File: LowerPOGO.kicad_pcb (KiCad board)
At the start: 2 copper layers, 116 x 67.1 mm, 29 parts, among them J1 Conn_01x01_MountingPin, J10 Conn_01x01_MountingPin, J11 Conn_01x01_MountingPin, J12 Conn_01x01_MountingPin, J13 Conn_01x01_MountingPin, J14 Conn_01x01_MountingPin, J15 Conn_01x01_MountingPin, J16 Conn_01x01_MountingPin, J17 Conn_01x01_MountingPin, J18 Conn_01x01_MountingPin, J19 Conn_01x01_MountingPin, J2 Conn_01x01_MountingPin, J20 Conn_01x01_MountingPin, J21 Conn_01x01_MountingPin, J22 Conn_01x01_MountingPin, J23 Conn_01x01_MountingPin, J24 Conn_01x01_MountingPin, J25 Conn_01x24_Pin, J3 Conn_01x01_MountingPin, J4 Conn_01x01_MountingPin, J5 Conn_01x01_MountingPin, J6 Conn_01x01_MountingPin, J7 Conn_01x01_MountingPin, J8 Conn_01x01_MountingPin, J9 Conn_01x01_MountingPin

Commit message: Update rev3 to modify J25 connector: Move J25 to be populated from the back of board Updated SVGs to show component 3D models Updated Fabrication Outputs
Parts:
- J25: moved to B.Cu
- moved J25 0.84 mm to (143.8, 91.7), turned to 180 degrees

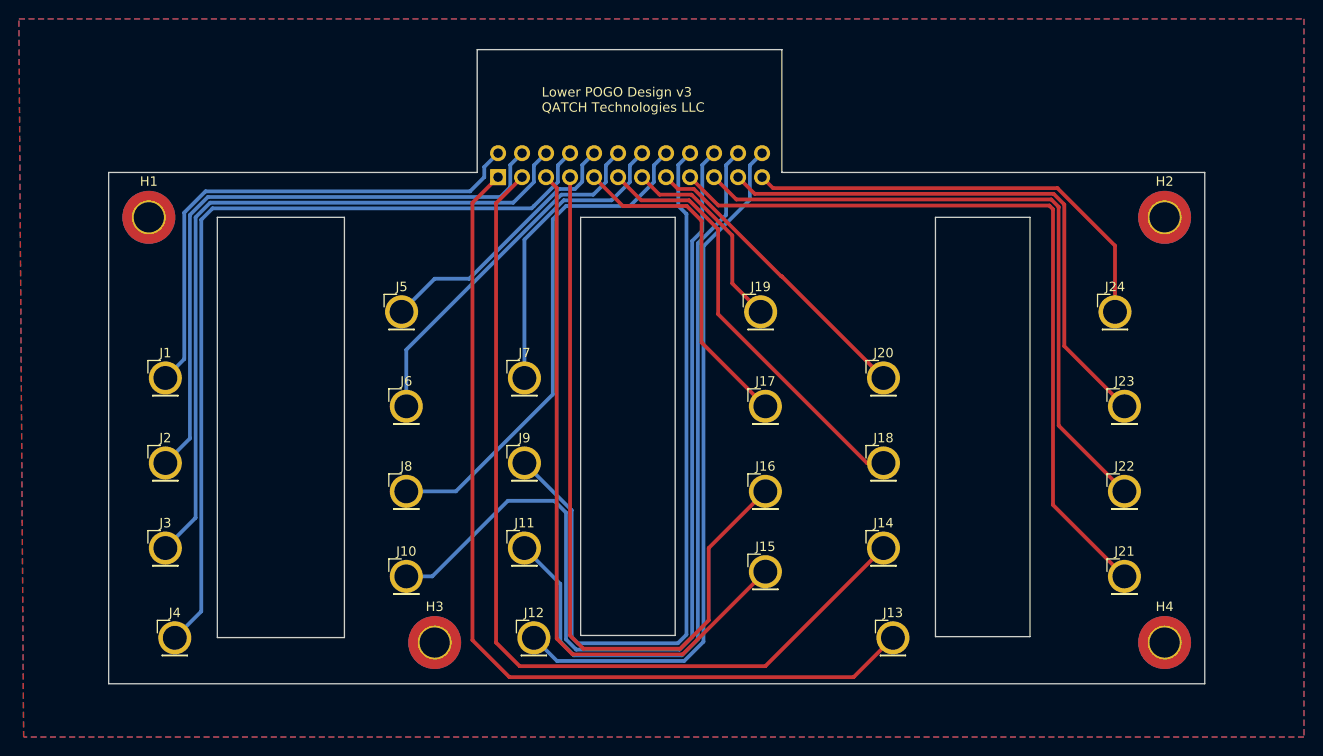
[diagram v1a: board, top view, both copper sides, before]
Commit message: LowerPOGO v4 (2024-06-21) Resize J vias for proper fit inner diameter: 2.49mm outer diameter: 3.25mm
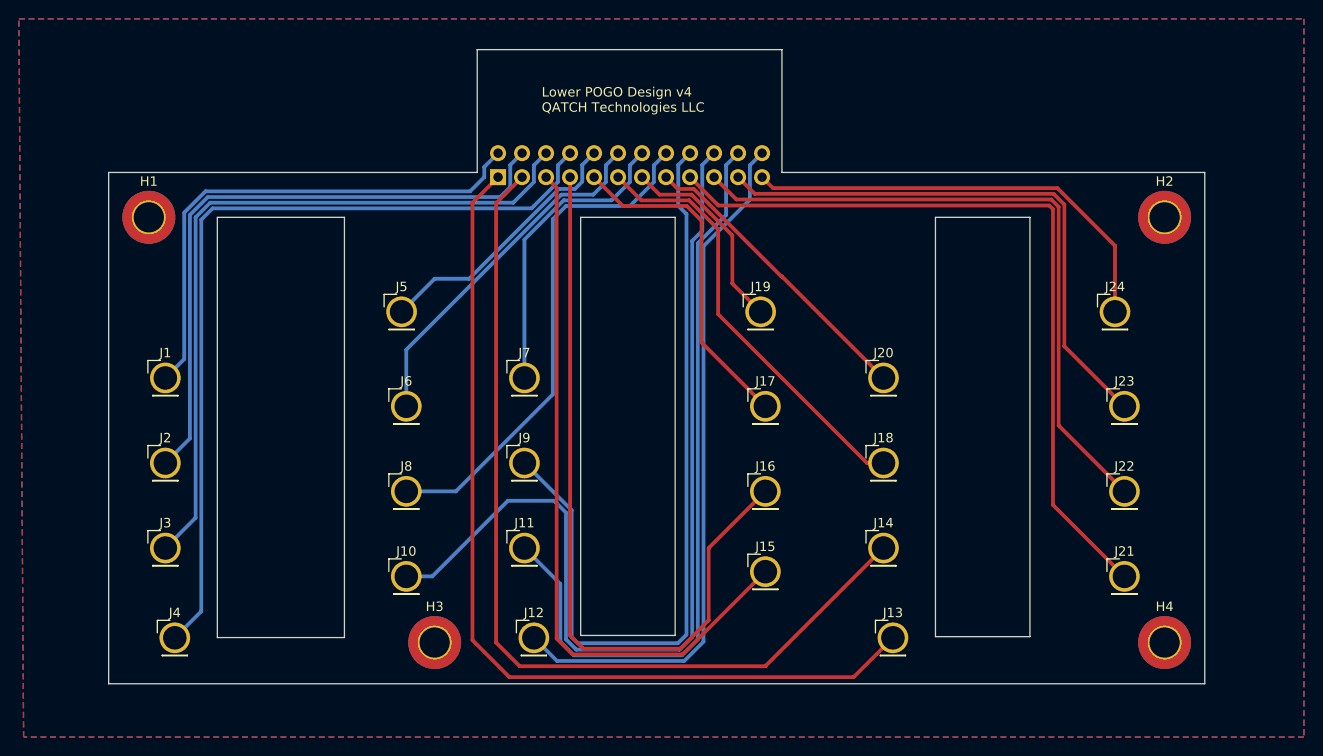
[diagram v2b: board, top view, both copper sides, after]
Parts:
- J1, J10, J11, J12, J13, J14, J15, J16, J17, J18, J19, J2, J20, J21, J22, J23, J24, J3, J4, J5, J6, J7, J8, J9: footprint Connector_PinHeader_2.54mm:PinHeader_1x01_D2.54mm_Vertical -> Connector_PinHeader_2.54mm:PinHeader_1x01_D2.54mm_Vertical_PogoPin
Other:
- board text added: "Lower POGO Design v4 QATCH Technologies LLC"
- board text removed: "Lower POGO Design v3 QATCH Technologies LLC"

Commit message: LowerPOGO v5 1mm trace spacing 1mm POGO clearance
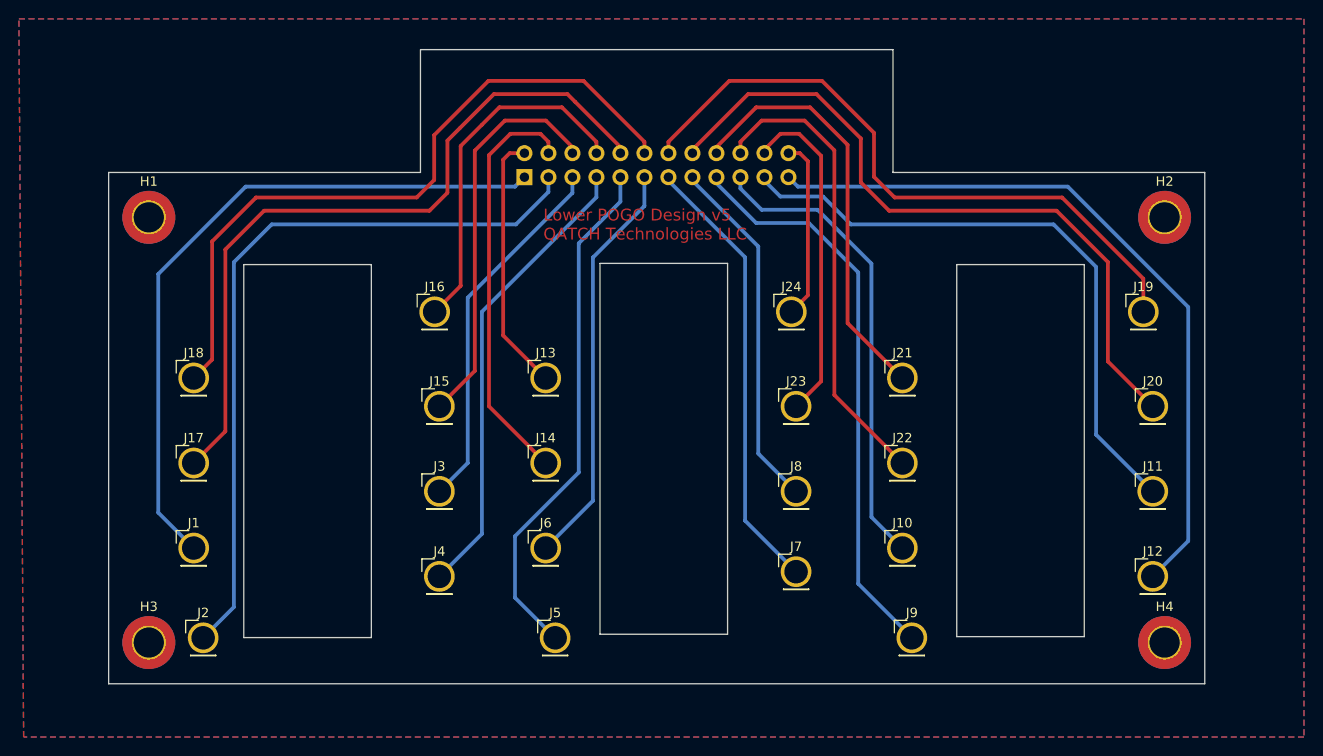
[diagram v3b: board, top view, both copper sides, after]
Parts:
- moved H3 30.2 mm to (93.2, 154.5)
- moved J15 3.50 mm to (124.0, 129.5)
- moved J16 3.50 mm to (123.5, 119.5)
- moved J3 3.50 mm to (124.0, 138.5)
- moved J4 3.50 mm to (124.0, 147.5)
- moved J23 3.25 mm to (161.8, 129.5)
- moved J24 3.25 mm to (161.2, 119.5)
- moved J7 3.25 mm to (161.8, 147.0)
- moved J8 3.25 mm to (161.8, 138.5)
- moved J1 3.00 mm to (98.0, 144.5)
- moved J11 3.00 mm to (199.5, 138.5)
- moved J12 3.00 mm to (199.5, 147.5)
- moved J17 3.00 mm to (98.0, 135.5)
- moved J18 3.00 mm to (98.0, 126.5)
- moved J19 3.00 mm to (198.5, 119.5)
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- renumbered J3 to J1, J14 to J10, J22 to J11, J21 to J12, J7 to J13, J9 to J14, J6 to J15, J5 to J16, J2 to J17, J1 to J18, J24 to J19, J4 to J2, J23 to J20, J20 to J21, J18 to J22, J17 to J23, J19 to J24, J8 to J3, J10 to J4, J12 to J5, J11 to J6, J15 to J7, J16 to J8, J13 to J9
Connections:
- J1 pad 1: Net-(J25-Pin_3) -> Net-(J1-Pin_1)
- J10 pad 1: Net-(J14-Pin_1) -> Net-(J10-Pin_1)
- J11 pad 1: Net-(J22-Pin_1) -> Net-(J11-Pin_1)
- J12 pad 1: Net-(J21-Pin_1) -> Net-(J12-Pin_1)
- J13 pad 1: Net-(J25-Pin_7) -> Net-(J13-Pin_1)
- J14 pad 1: Net-(J25-Pin_9) -> Net-(J14-Pin_1)
- J15 pad 1: Net-(J25-Pin_6) -> Net-(J15-Pin_1)
- J16 pad 1: Net-(J25-Pin_5) -> Net-(J16-Pin_1)
- J17 pad 1: Net-(J2-Pin_1) -> Net-(J17-Pin_1)
- J18 pad 1: Net-(J1-Pin_1) -> Net-(J18-Pin_1)
- J19 pad 1: Net-(J24-Pin_1) -> Net-(J19-Pin_1)
- J2 pad 1: Net-(J25-Pin_4) -> Net-(J2-Pin_1)
- J20 pad 1: Net-(J23-Pin_1) -> Net-(J20-Pin_1)
- J21 pad 1: Net-(J20-Pin_1) -> Net-(J21-Pin_1)
- J22 pad 1: Net-(J18-Pin_1) -> Net-(J22-Pin_1)
- J23 pad 1: Net-(J17-Pin_1) -> Net-(J23-Pin_1)
- J24 pad 1: Net-(J19-Pin_1) -> Net-(J24-Pin_1)
- J3 pad 1: Net-(J25-Pin_8) -> Net-(J25-Pin_3)
- J4 pad 1: Net-(J10-Pin_1) -> Net-(J25-Pin_4)
- J5 pad 1: Net-(J12-Pin_1) -> Net-(J25-Pin_5)
- J6 pad 1: Net-(J11-Pin_1) -> Net-(J25-Pin_6)
- J7 pad 1: Net-(J15-Pin_1) -> Net-(J25-Pin_7)
- J8 pad 1: Net-(J16-Pin_1) -> Net-(J25-Pin_8)
- J9 pad 1: Net-(J13-Pin_1) -> Net-(J25-Pin_9)
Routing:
- net Net-(J13-Pin_1): track 98.0 -> 27.6 mm
- net Net-(J14-Pin_1): track 97.6 -> 43.8 mm
- net Net-(J10-Pin_1): track 100.7 -> 49.8 mm
- net Net-(J19-Pin_1): track 21.4 -> 69.0 mm
- net Net-(J16-Pin_1): track 81.1 -> 37.5 mm
- net Net-(J17-Pin_1): track 35.7 -> 78.8 mm
- net Net-(J20-Pin_1): track 31.8 -> 74.1 mm
- net Net-(J25-Pin_4): track 88.4 -> 49.1 mm
- net Net-(J25-Pin_3): track 77.3 -> 39.1 mm
- net Net-(J21-Pin_1): track 81.8 -> 45.0 mm
- net Net-(J15-Pin_1): track 75.7 -> 42.1 mm
- net Net-(J18-Pin_1): track 45.9 -> 74.7 mm
- net Net-(J24-Pin_1): track 47.4 -> 19.1 mm
- net Net-(J25-Pin_5): track 28.4 -> 55.1 mm
- net Net-(J25-Pin_9): track 85.1 -> 60.6 mm
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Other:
- outline, holes or cut-outs redrawn
- board text added: "Lower POGO Design v5 QATCH Technologies LLC"
- board text removed: "Lower POGO Design v4 QATCH Technologies LLC"

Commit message: Changes for LowerPOGO v6: - Move the 3 cutouts left 2.5mm - Reduce cutout height by 1.5mm - Move center port right 0.25mm - Move traces for moved cutouts - Set clearance to avoid island - Update version text to "v6" - Update fabrication outputs - Update dimensional drawing
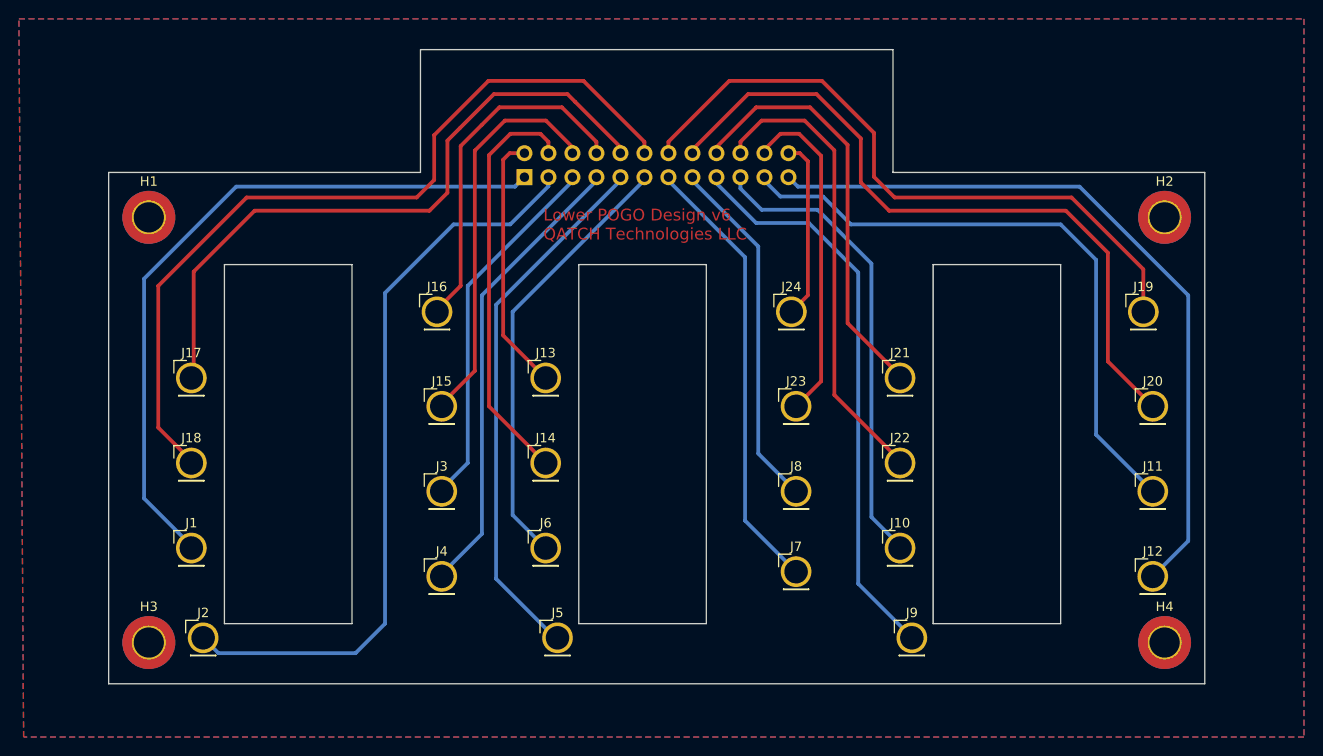
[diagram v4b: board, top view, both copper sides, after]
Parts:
- moved J1 0.25 mm to (97.8, 144.5)
- moved J10 0.25 mm to (172.8, 144.5)
- moved J15 0.25 mm to (124.2, 129.5)
- moved J16 0.25 mm to (123.8, 119.5)
- moved J17 0.25 mm to (97.8, 126.5)
- moved J18 0.25 mm to (97.8, 135.5)
- moved J21 0.25 mm to (172.8, 126.5)
- moved J22 0.25 mm to (172.8, 135.5)
- moved J3 0.25 mm to (124.2, 138.5)
- moved J4 0.25 mm to (124.2, 147.5)
- moved J5 0.25 mm to (136.5, 154.0)
- renumbered J18 to J17, J17 to J18
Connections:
- J17 pad 1: Net-(J18-Pin_1) -> Net-(J17-Pin_1)
- J18 pad 1: Net-(J17-Pin_1) -> Net-(J18-Pin_1)
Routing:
- net Net-(J18-Pin_1): track 74.7 -> 87.4 mm
- net Net-(J17-Pin_1): track 78.8 -> 70.4 mm
- net Net-(J25-Pin_6): track 43.6 -> 46.5 mm
- net Net-(J1-Pin_1): track 73.5 -> 75.4 mm
- net Net-(J25-Pin_5): track 55.1 -> 56.8 mm
- net Net-(J12-Pin_1): track 78.1 -> 78.8 mm
- net Net-(J19-Pin_1): track 69.0 -> 69.6 mm
- net Net-(J20-Pin_1): track 74.1 -> 74.7 mm
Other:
- outline, holes or cut-outs redrawn
- board text added: "Lower POGO Design v6 QATCH Technologies LLC"
- board text removed: "Lower POGO Design v5 QATCH Technologies LLC"

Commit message: Pushing local changes before branching
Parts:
- moved J25 2.21 mm to (146.5, 89.5)
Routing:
- net Net-(J22-Pin_1): track 49.5 -> 51.7 mm
- net Net-(J25-Pin_9): track 60.6 -> 62.8 mm
- net Net-(J25-Pin_7): track 47.3 -> 49.6 mm
- net Net-(J12-Pin_1): track 78.8 -> 81.0 mm
- net Net-(J11-Pin_1): track 65.9 -> 68.1 mm
- net Net-(J25-Pin_8): track 37.8 -> 40.0 mm
- net Net-(J25-Pin_6): track 46.5 -> 48.7 mm
- net Net-(J25-Pin_4): track 49.1 -> 51.3 mm
- net Net-(J25-Pin_3): track 39.1 -> 41.3 mm
- net Net-(J1-Pin_1): track 75.4 -> 77.6 mm
- net Net-(J25-Pin_5): track 56.8 -> 59.0 mm
- net Net-(J18-Pin_1): track 87.4 -> 89.6 mm
- net Net-(J21-Pin_1): track 45.0 -> 47.2 mm
- net Net-(J16-Pin_1): track 37.5 -> 39.6 mm
- net Net-(J15-Pin_1): track 42.1 -> 44.2 mm
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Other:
- board size 116 x 67.1 mm -> 116 x 69 mm

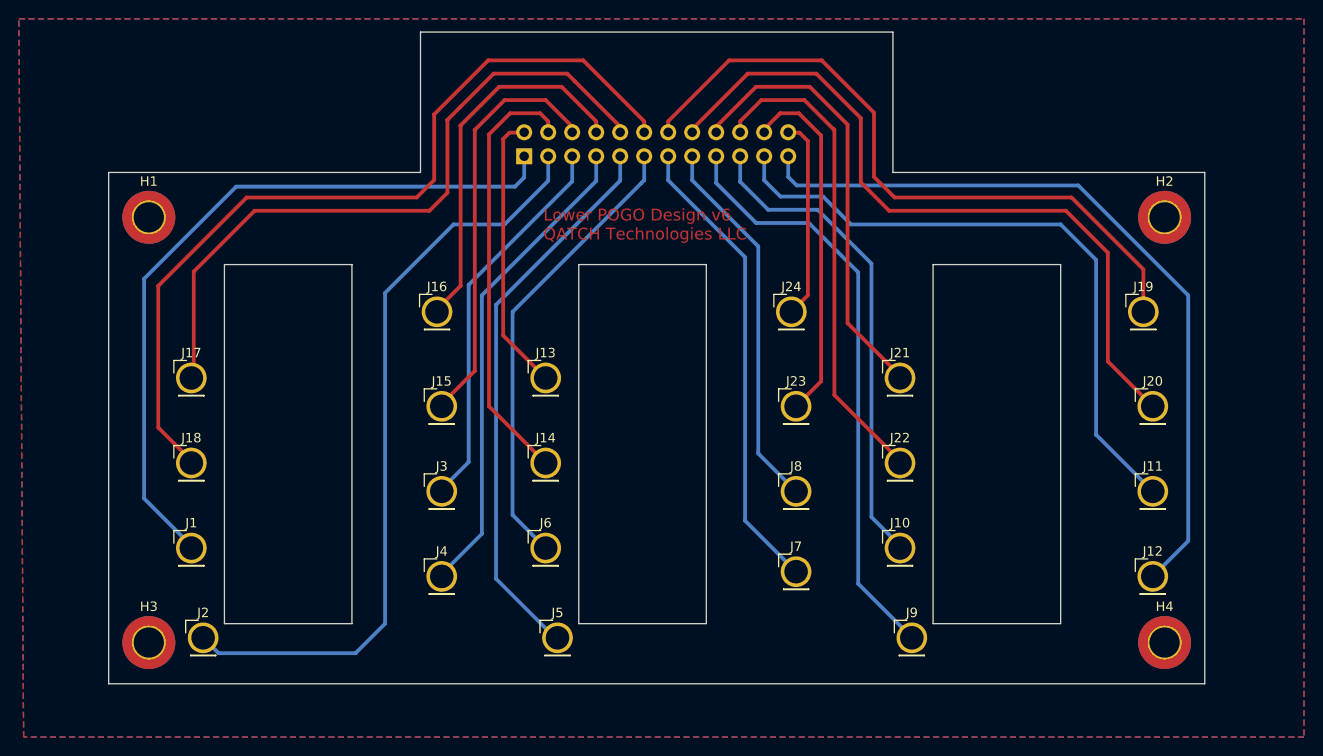
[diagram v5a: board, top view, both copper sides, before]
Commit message: Update KiCad designs for LowerPOGO to Multiport Design (v7) Tag fabrication outputs for this revision, remove Drawings.
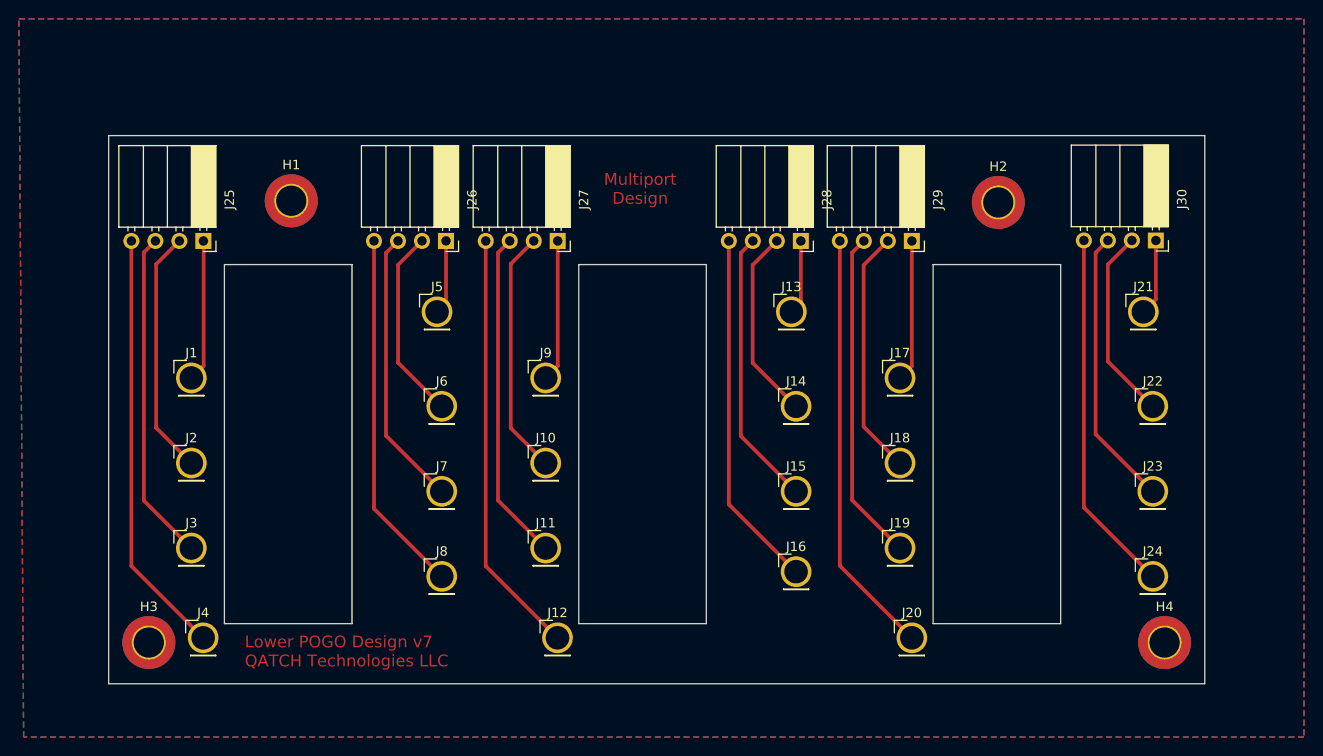
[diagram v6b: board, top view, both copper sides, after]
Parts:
- added J26: Conn_01x04_Pin, Connector_PinSocket_2.54mm:PinSocket_1x04_P2.54mm_Horizontal, F.Cu at (124.7, 112.0)
- added J27: Conn_01x04_Pin, Connector_PinSocket_2.54mm:PinSocket_1x04_P2.54mm_Horizontal, F.Cu at (136.5, 112.0)
- added J28: Conn_01x04_Pin, Connector_PinSocket_2.54mm:PinSocket_1x04_P2.54mm_Horizontal, F.Cu at (162.2, 112.0)
- added J29: Conn_01x04_Pin, Connector_PinSocket_2.54mm:PinSocket_1x04_P2.54mm_Horizontal, F.Cu at (174.0, 112.0)
- added J30: Conn_01x04_Pin, Connector_PinSocket_2.54mm:PinSocket_1x04_P2.54mm_Horizontal, F.Cu at (199.8, 112.0)
- J25: value Conn_01x24_Pin -> Conn_01x04_Pin; footprint Connector_PinSocket_2.54mm:PinSocket_2x12_P2.54mm_Horizontal -> Connector_PinSocket_2.54mm:PinSocket_1x04_P2.54mm_Horizontal; moved to F.Cu
- moved J25 52.6 mm to (99.0, 112.0), turned to -90 degrees
- moved H2 17.7 mm to (183.2, 107.9)
- moved H1 15.2 mm to (108.3, 107.8)
- renumbered J17 to J1, J14 to J10, J6 to J11, J5 to J12, J24 to J13, J23 to J14, J8 to J15, J7 to J16, J21 to J17, J22 to J18, J10 to J19, J18 to J2, J9 to J20, J19 to J21, J20 to J22, J11 to J23, J12 to J24, J1 to J3, J2 to J4, J16 to J5, J15 to J6, J3 to J7, J4 to J8, J13 to J9
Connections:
- J1 pad 1: Net-(J17-Pin_1) -> Net-(J1-Pin_1)
- J10 pad 1: Net-(J14-Pin_1) -> Net-(J10-Pin_1)
- J11 pad 1: Net-(J25-Pin_6) -> Net-(J11-Pin_1)
- J12 pad 1: Net-(J25-Pin_5) -> Net-(J12-Pin_1)
- J13 pad 1: Net-(J24-Pin_1) -> Net-(J13-Pin_1)
- J14 pad 1: Net-(J23-Pin_1) -> Net-(J14-Pin_1)
- J15 pad 1: Net-(J25-Pin_8) -> Net-(J15-Pin_1)
- J16 pad 1: Net-(J25-Pin_7) -> Net-(J16-Pin_1)
- J17 pad 1: Net-(J21-Pin_1) -> Net-(J17-Pin_1)
- J18 pad 1: Net-(J22-Pin_1) -> Net-(J18-Pin_1)
- J19 pad 1: Net-(J10-Pin_1) -> Net-(J19-Pin_1)
- J2 pad 1: Net-(J18-Pin_1) -> Net-(J2-Pin_1)
- J20 pad 1: Net-(J25-Pin_9) -> Net-(J20-Pin_1)
- J21 pad 1: Net-(J19-Pin_1) -> Net-(J21-Pin_1)
- J22 pad 1: Net-(J20-Pin_1) -> Net-(J22-Pin_1)
- J23 pad 1: Net-(J11-Pin_1) -> Net-(J23-Pin_1)
- J24 pad 1: Net-(J12-Pin_1) -> Net-(J24-Pin_1)
- J3 pad 1: Net-(J1-Pin_1) -> Net-(J25-Pin_3)
- J4 pad 1: Net-(J2-Pin_1) -> Net-(J25-Pin_4)
- J5 pad 1: Net-(J16-Pin_1) -> Net-(J26-Pin_1)
- J6 pad 1: Net-(J15-Pin_1) -> Net-(J26-Pin_2)
- J7 pad 1: Net-(J25-Pin_3) -> Net-(J26-Pin_3)
- J8 pad 1: Net-(J25-Pin_4) -> Net-(J26-Pin_4)
- J9 pad 1: Net-(J13-Pin_1) -> Net-(J27-Pin_1)
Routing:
- net Net-(J18-Pin_1): track 89.6 -> 26.2 mm
- net Net-(J25-Pin_9): track 62.8 -> 0.00 mm
- net Net-(J1-Pin_1): track 77.6 -> 15.0 mm
- net Net-(J25-Pin_5): track 59.0 -> 0.00 mm
- net Net-(J17-Pin_1): track 72.6 -> 15.0 mm
- net Net-(J2-Pin_1): track 81.0 -> 26.1 mm
- net Net-(J25-Pin_7): track 49.6 -> 0.00 mm
- net Net-(J25-Pin_6): track 48.7 -> 0.00 mm
- net Net-(J25-Pin_8): track 40.0 -> 0.00 mm
- net Net-(J21-Pin_1): track 47.2 -> 8.10 mm
- net Net-(J26-Pin_4): track 0.00 -> 38.5 mm
- net Net-(J19-Pin_1): track 71.8 -> 35.1 mm
- net Net-(J12-Pin_1): track 81.0 -> 45.1 mm
- net Net-(J11-Pin_1): track 68.1 -> 35.1 mm
- net Net-(J20-Pin_1): track 76.8 -> 45.2 mm
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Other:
- board size 116 x 69 mm -> 116 x 58 mm
- board text added: "Lower POGO Design v7 QATCH Technologies LLC"
- board text added: "Multiport Design"
- board text removed: "Lower POGO Design v6 QATCH Technologies LLC"
